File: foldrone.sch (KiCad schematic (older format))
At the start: 48 parts, among them IC1 ATMEGA328P-M, Q1 STS5NF60L, Q2 STS5NF60L, Q3 STS5NF60L, Q4 STS5NF60L, SW1 Reset, SW2 LimitSW, U1 3.3_lod, U2 TLV1117-33IDCY, U3 MPU-6050, m1 motor, m2 motor, m3 motor, m4 motor

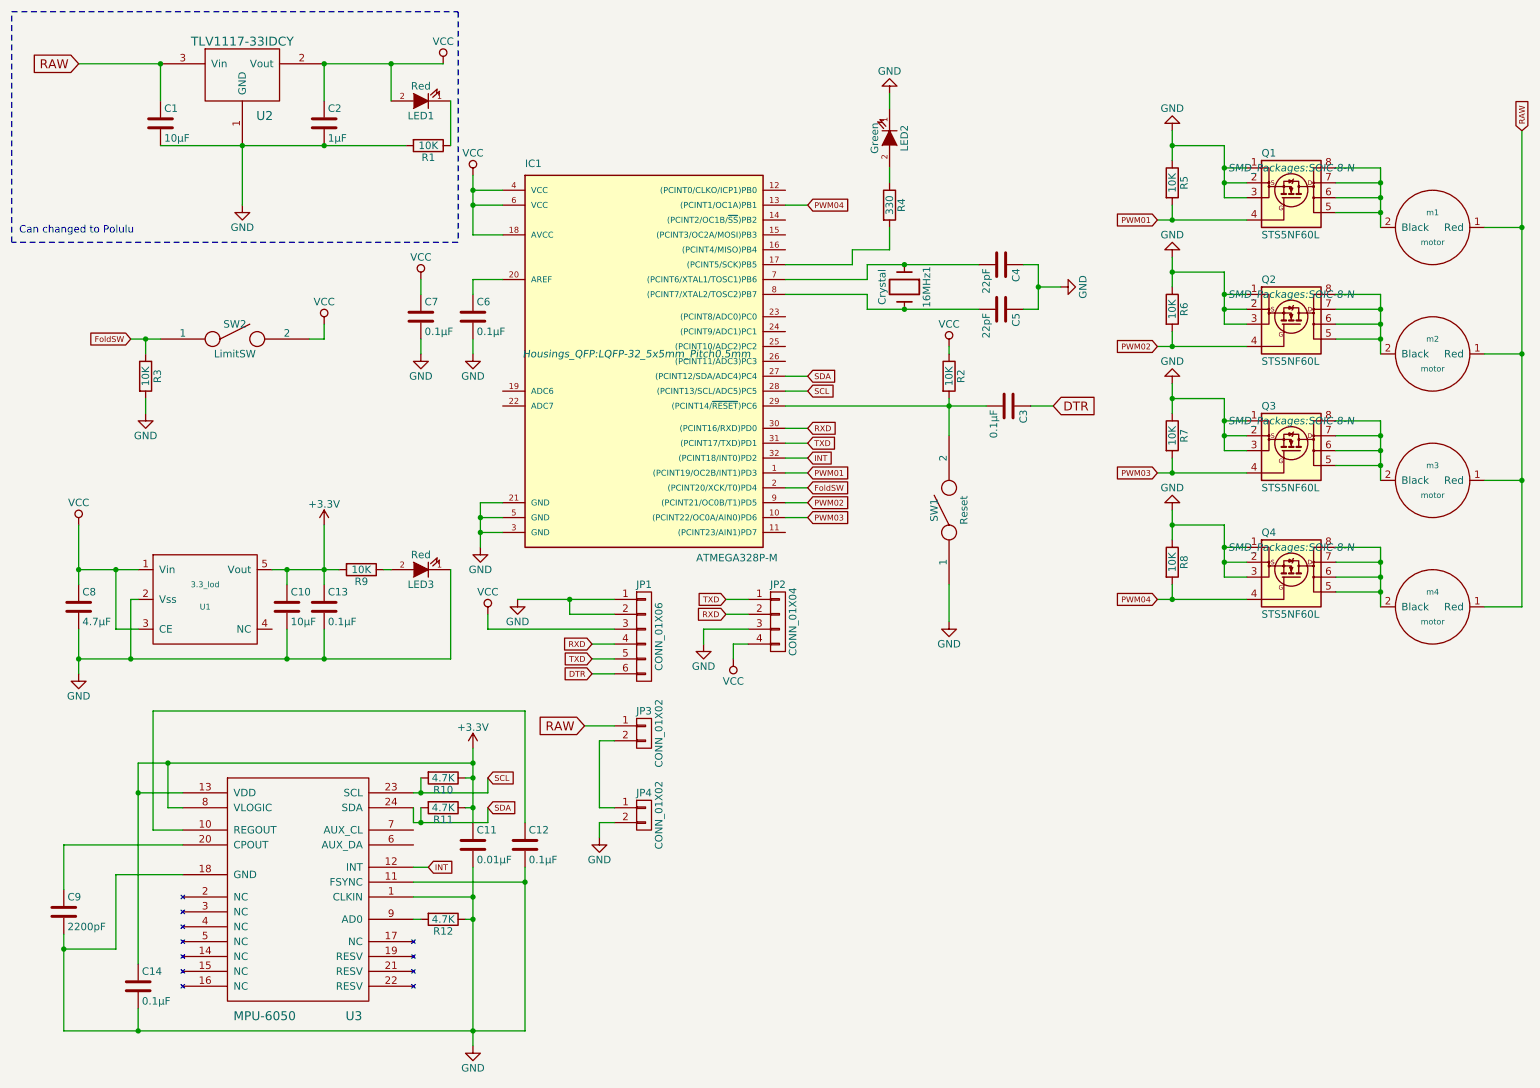
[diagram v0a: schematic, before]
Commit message: Proto PCB ready
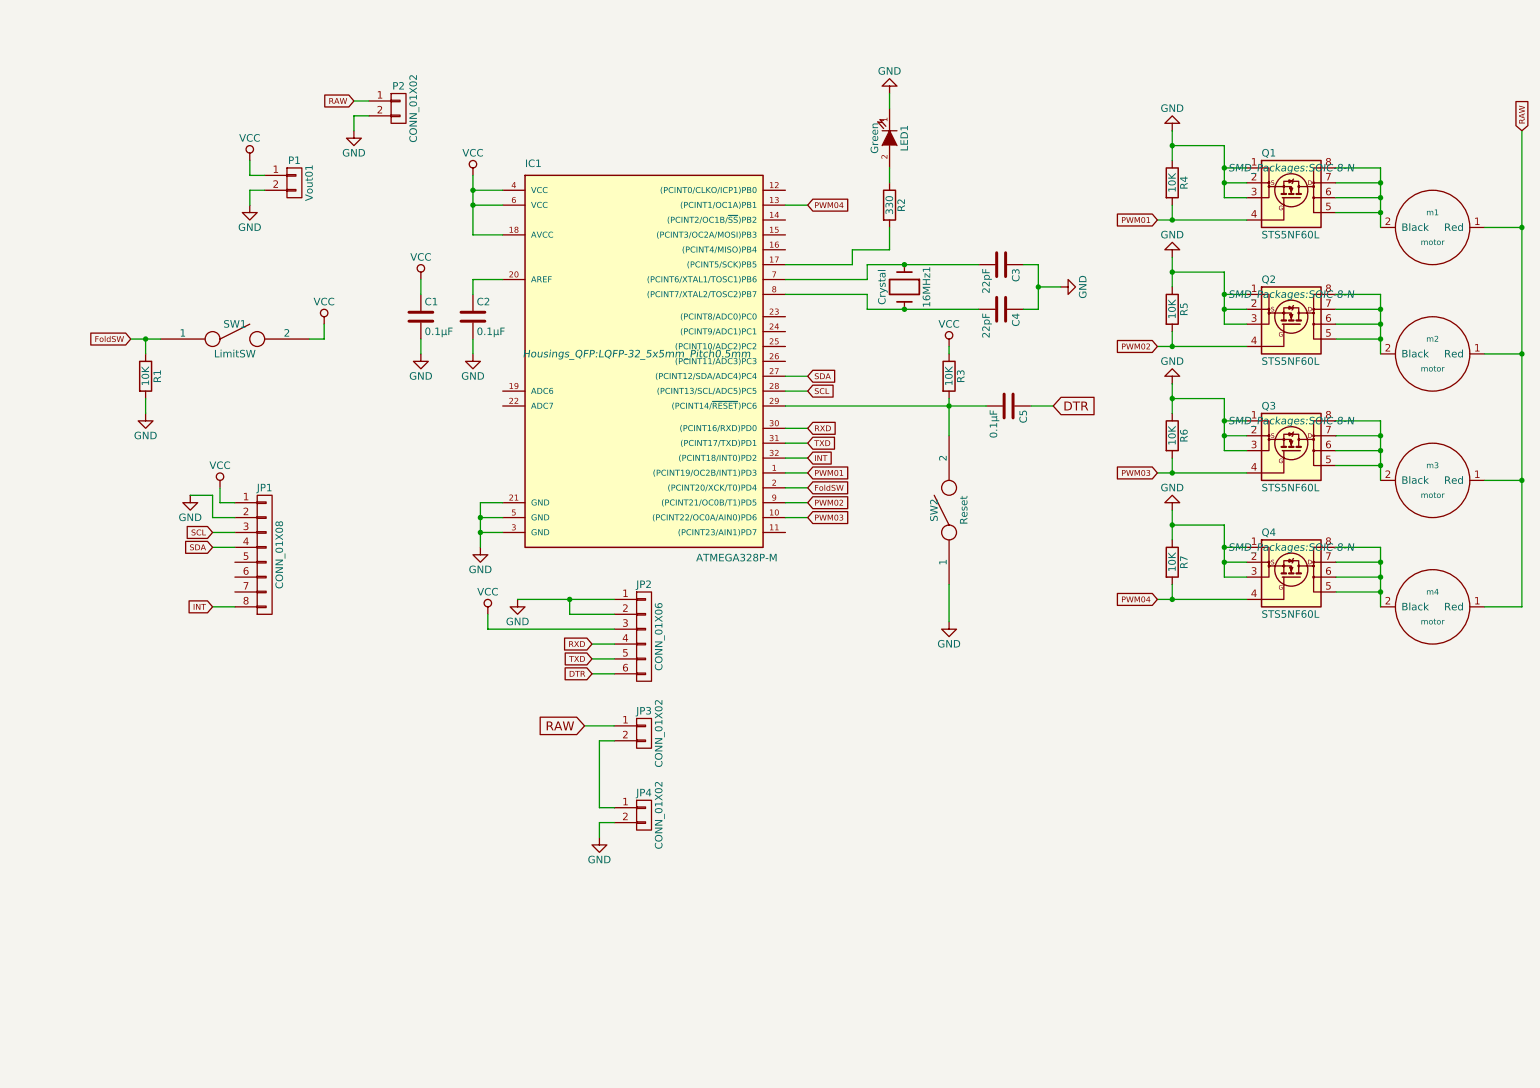
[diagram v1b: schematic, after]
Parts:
- removed C1, C10: 10μF, Capacitors_SMD:C_0603_HandSoldering, symbol C
- removed C11: 0.01μF, Capacitors_SMD:C_0603_HandSoldering, symbol C
- removed C12, C13, C14: 0.1μF, Capacitors_SMD:C_0603_HandSoldering, symbol C
- removed C2: 1μF, Capacitors_SMD:C_0603_HandSoldering, symbol C
- removed C8: 4.7μF, Capacitors_SMD:C_0603_HandSoldering, symbol C
- removed C9: 2200pF, Capacitors_SMD:C_0603_HandSoldering, symbol C
- removed JP2: CONN_01X04, Connectors_Molex:Molex_PicoBlade_53047-0410, symbol CONN_01X04
- removed LED1, LED3: Red, LEDs:LED_0603, symbol LED
- removed R1, R9: 10K, Resistors_SMD:R_0603_HandSoldering, symbol R
- removed R10, R11, R12: 4.7K, Resistors_SMD:R_0603_HandSoldering, symbol R
- removed U1: 3.3_lod, TO_SOT_Packages_SMD:SOT-23-5, symbol 3.3_lod
- removed U2: TLV1117-33IDCY, TO_SOT_Packages_SMD:SOT-223, symbol TLV1117-33IDCY
- removed U3: MPU-6050, Housings_DFN_QFN:QFN-24-1EP_4x4mm_Pitch0.5mm, symbol MPU-6050
- added JP1: CONN_01X08, Socket_Strips:Socket_Strip_Straight_1x08, symbol CONN_01X08
- added P1: Vout01, Socket_Strips:Socket_Strip_Straight_1x02, symbol CONN_01X02
- added P2: CONN_01X02, Socket_Strips:Socket_Strip_Straight_1x02, symbol CONN_01X02
- JP2: renamed from JP1; footprint Connectors_Molex:Molex_PicoBlade_53047-0610 -> Socket_Strips:Socket_Strip_Straight_1x06
- m1, m2, m3, m4: footprint Connectors_Molex:Molex_PicoBlade_53047-0210 -> Socket_Strips:Socket_Strip_Straight_1x02
- renumbered C7 to C1, C6 to C2, C4 to C3, C5 to C4, C3 to C5, LED2 to LED1, R3 to R1, R4 to R2, R2 to R3, R5 to R4, R6 to R5, R7 to R6, R8 to R7, SW2 to SW1, SW1 to SW2
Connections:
- net GND: now also JP1.2 (P2), P1.2 (P2), P2.2 (P2)
- net INT: now also JP1.8 (P8)
- net RAW: now also P2.1 (P1)
- net SCL: now also JP1.3 (P3)
- net SDA: now also JP1.4 (P4)
- net VCC: now also JP1.1 (P1), P1.1 (P1)
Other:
- note removed: "Can changed to Polulu"
